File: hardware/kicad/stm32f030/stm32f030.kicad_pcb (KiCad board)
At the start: 2 copper layers, 29.6 x 10 mm, 89 parts, among them IC1 AT24CS02-SSHM, K1 RELAY_1RT, K2 RELAY_1RT, P1 5VIN, P10 SWD, P2 LOOP1, P3 LOOP2, P4 RELAY OUT 1, P5 TTL OUT 1, P6 RELAY OUT 2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

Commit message: hardware/kicad/stm32f030: blocks ready
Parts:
- C10, C14, C15, Q4, R10, R11, R12, R28: moved to B.Cu
- Y1: value 12MHz -> 8MHz; footprint Crystals:Crystal_SMD_3225_4Pads -> Crystals:Crystal_HC49-4H_Vertical
- moved K2 41.2 mm to (11.2, 150.4)
- moved LED2 41.1 mm to (15.7, 125.5)
- moved P7 41.1 mm to (11.7, 121.9)
- moved Q7 41.1 mm to (17.3, 130.0)
- moved Q8 41.1 mm to (17.3, 130.0)
- moved R20 41.1 mm to (20.3, 123.7)
- moved R21 41.1 mm to (15.7, 123.7)
- moved R22 41.1 mm to (20.3, 127.3)
- moved R23 41.1 mm to (20.3, 125.5)
- moved R24 41.1 mm to (15.7, 127.3)
- moved D2 41.1 mm to (23.1, 131.3)
- moved SW2 41.1 mm to (22.6, 121.2)
- moved P6 41.1 mm to (17.3, 158.0)
- moved P5 33.4 mm to (107.7, 125.1)
- moved D1 32.8 mm to (118.6, 131.6)
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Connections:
- P3 pad 1: Net-(GDT3-Pad2) -> Net-(GDT3-Pad1)
- P3 pad 3: Net-(GDT3-Pad1) -> Net-(GDT3-Pad2)
- R11 pad 1: /colpitts/osc1 -> /MCU/osc1
- R18 pad 2: /outputs/active1 -> /MCU/active1
- R23 pad 2: /MCU/active1 -> /MCU/active2
- R4 pad 1: /MCU/osc1 -> /MCU/osc2
- T2 pad 1: Net-(JP2-Pad2) -> Net-(C10-Pad1)
- T2 pad 3: Net-(C10-Pad1) -> Net-(JP2-Pad2)
- T2 pad 4: Net-(GDT3-Pad2) -> Net-(GDT3-Pad1)
- T2 pad 6: Net-(GDT3-Pad1) -> Net-(GDT3-Pad2)
- U2 pad 13: /colpitts/osc1 -> /MCU/osc2
- U2 pad 14: /outputs/active1 -> /MCU/active2
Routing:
- net +3V3: track 49.8 -> 19.0 mm
- net +5V: track 74.3 -> 91.4 mm, vias 1 -> 2
- net /MCU/active2: track 0.00 -> 16.5 mm, vias 0 -> 2
- net /MCU/active1: track 12.5 -> 0.40 mm, vias 1 -> 0
- net Net-(C15-Pad1): track 5.02 -> 16.4 mm
- net /colpitts/osc1: track 7.79 -> 0.00 mm, vias 1 -> 0
- net /MCU/osc2: track 0.00 -> 7.79 mm, vias 0 -> 1
- net Net-(JP3-Pad2): track 6.90 -> 14.6 mm
- net Net-(C10-Pad1): track 37.3 -> 30.5 mm, vias 0 -> 1
- net Net-(C14-Pad1): track 15.8 -> 11.2 mm
- net /MCU/reset: track 30.7 -> 26.3 mm, vias 2 -> 1
- net /outputs/active1: track 4.37 -> 0.00 mm, vias 1 -> 0
- net Net-(LED1-Pad1): track 14.1 -> 9.71 mm
- net Net-(Q4-Pad1): track 5.81 -> 1.58 mm
- net Net-(JP2-Pad2): track 24.3 -> 20.2 mm
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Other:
- board size 29.6 x 10 mm -> 103.5 x 10 mm

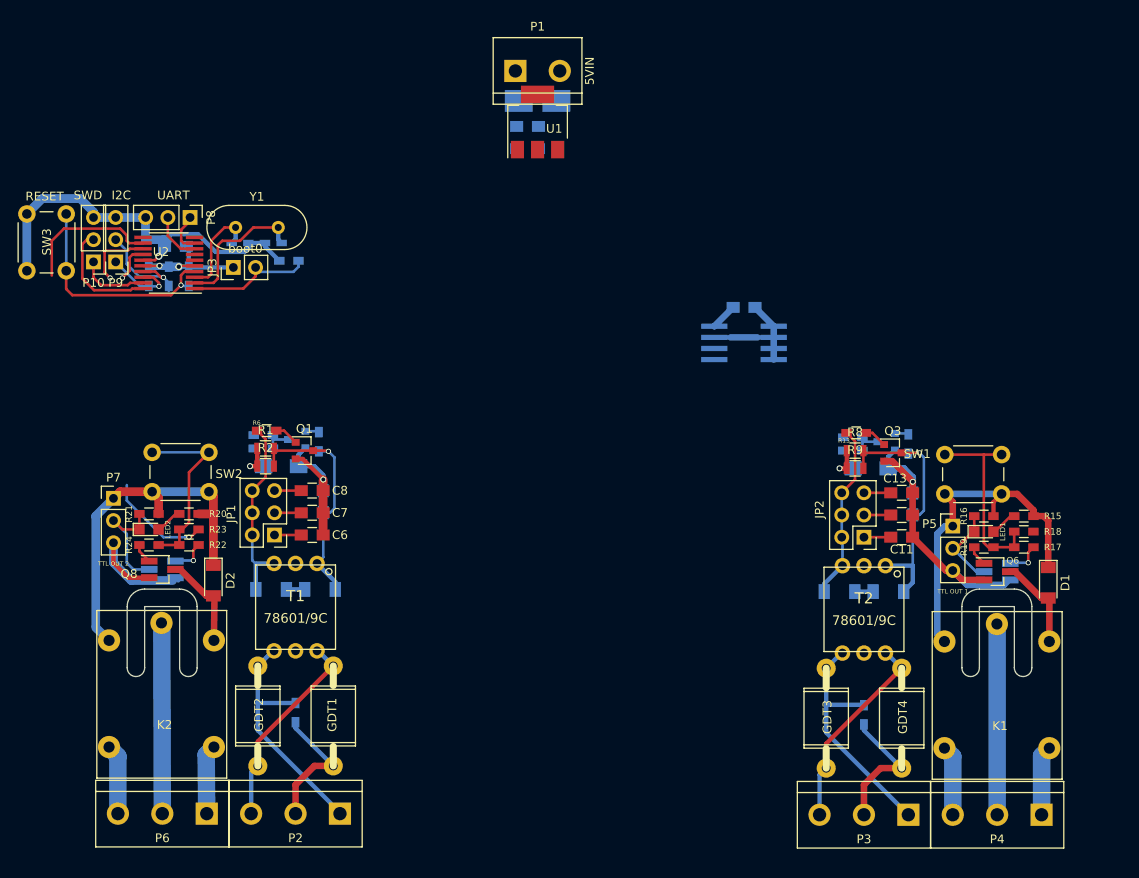
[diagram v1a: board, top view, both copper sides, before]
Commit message: hardware/kicad/stm32f030: everything is connected, DRC OK
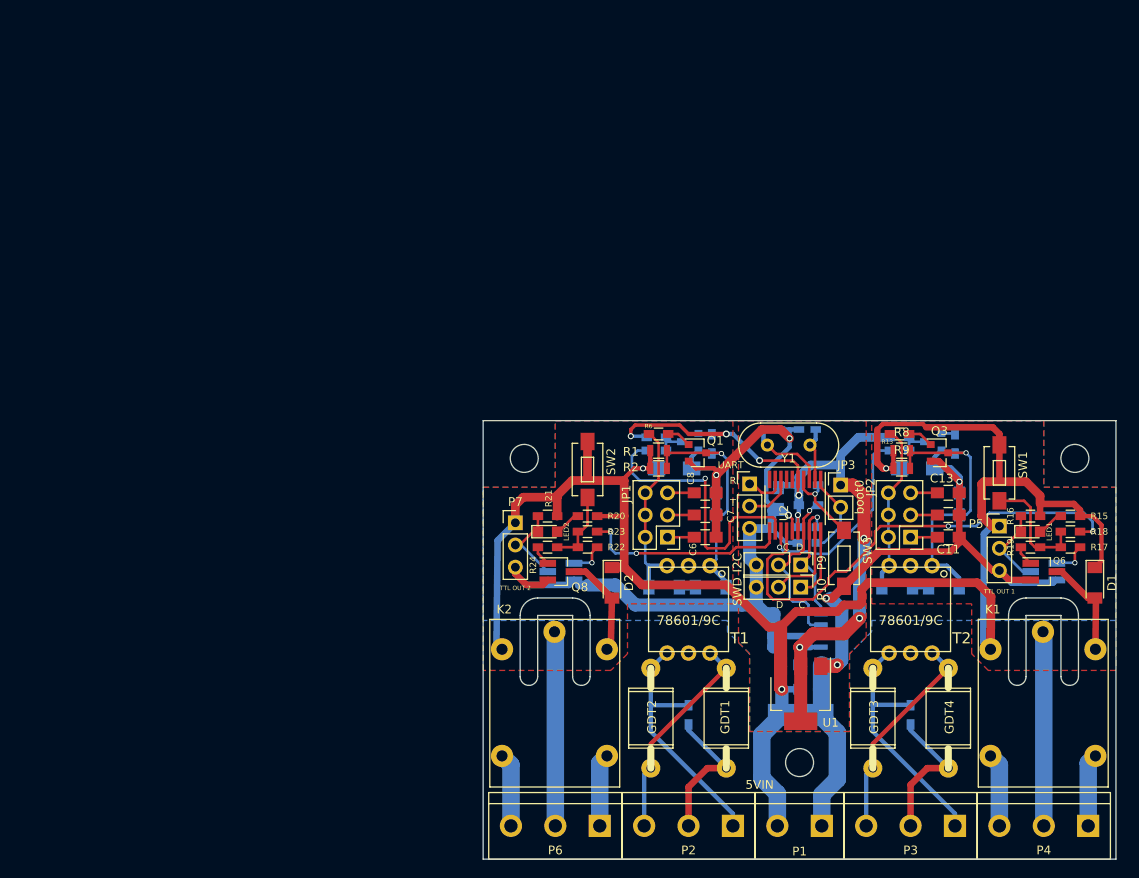
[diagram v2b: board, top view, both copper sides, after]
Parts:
- removed C18: 100n, Capacitors_SMD:C_0805_HandSoldering
- added REF**: MountingHole_3.2mm_M3, Mounting_Holes:MountingHole_3.2mm_M3, F.Cu at (90.2, 152.1)
- added REF**: MountingHole_3.2mm_M3, Mounting_Holes:MountingHole_3.2mm_M3, F.Cu at (121.7, 117.3)
- added REF**: MountingHole_3.2mm_M3, Mounting_Holes:MountingHole_3.2mm_M3, F.Cu at (58.7, 117.3)
- SW1, SW2: value TACTILE_SW -> SW_Push; footprint Buttons_Switches_THT:SW_PUSH_6mm -> cardetector:TS_362
- SW3: value RESET -> SW_Push; footprint Buttons_Switches_THT:SW_PUSH_6mm -> cardetector:TS_362
- moved SW3 99.1 mm to (95.2, 128.8), turned to 270 degrees
- moved P1 91.4 mm to (90.2, 159.4), turned to 180 degrees
- moved P10 89.0 mm to (90.3, 132.1), turned to 270 degrees
- moved P9 85.7 mm to (90.3, 129.5), turned to 270 degrees
- moved R27 80.6 mm to (91.1, 125.2), turned to 0 degrees
- moved R26 77.7 mm to (91.2, 122.7), turned to 0 degrees
- moved U2 76.8 mm to (89.7, 122.7), turned to 270 degrees
- moved C1 76.4 mm to (90.3, 146.7), turned to 0 degrees
- moved R25 74.8 mm to (91.2, 120.4), turned to 0 degrees
- moved C16 74.8 mm to (87.8, 121.9), turned to 270 degrees
- moved JP3 73.8 mm to (94.9, 120.4), turned to 0 degrees
- moved C2 72.1 mm to (91.4, 143.8), turned to 0 degrees
- moved U1 72.0 mm to (90.3, 144.3), turned to 270 degrees
- moved P8 70.9 mm to (84.5, 120.3), turned to 0 degrees
- moved R28 67.5 mm to (91.1, 127.0)
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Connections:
- P10 pad 1: /MCU/SWD -> /MCU/SWC
- P10 pad 2: /MCU/SWC -> /MCU/SWD
- R11 pad 1: /MCU/osc1 -> /MCU/osc2
- R18 pad 2: /MCU/active1 -> /MCU/active2
- R23 pad 2: /MCU/active2 -> /MCU/active1
- R4 pad 1: /MCU/osc2 -> /MCU/osc1
- SW3 pad 1: GND -> /MCU/reset
- SW3 pad 2: /MCU/reset -> GND
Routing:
- net +5V: track 91.4 -> 216.0 mm, vias 2 -> 3
- net +3V3: track 19.0 -> 91.4 mm, vias 2 -> 8
- net GND: track 135.4 -> 201.6 mm, vias 3 -> 6
- net /MCU/active2: track 16.5 -> 54.5 mm
- net /MCU/active1: track 0.40 -> 23.8 mm, vias 0 -> 2
- net /MCU/reset: track 26.3 -> 9.45 mm
- net /MCU/osc1: track 16.1 -> 32.8 mm, vias 0 -> 1
- net /MCU/osc2: track 7.79 -> 23.4 mm
- net Net-(R22-Pad2): track 21.1 -> 8.72 mm
- net Net-(C15-Pad1): track 16.4 -> 6.21 mm
- net Net-(R17-Pad2): track 22.0 -> 13.4 mm
- net /EEPROM/scl: track 12.7 -> 20.5 mm
- net /EEPROM/sda: track 9.10 -> 14.6 mm
- net /MCU/SWC: track 13.0 -> 8.12 mm
- net Net-(JP3-Pad2): track 14.6 -> 9.78 mm
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- added copper zone on F.Cu, net +3V3
- added copper zone on F.Cu, net +5V
- added copper zone on B.Cu, net GND
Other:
- board size 103.5 x 10 mm -> 72.4 x 50.2 mm
- board text added: "C"
- board text added: "D"
- board text added: "R"
- board text added: "T"

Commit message: hardware/kicad/stm32f030: final touches
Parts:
- moved REF** 0.28 mm to (121.9, 117.5)
- moved REF** 0.28 mm to (58.4, 117.5)
- moved C1 0.25 mm to (90.3, 146.9)
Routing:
- net /EEPROM/scl: track 20.5 -> 19.6 mm
- removed copper zone on F.Cu, net +3V3

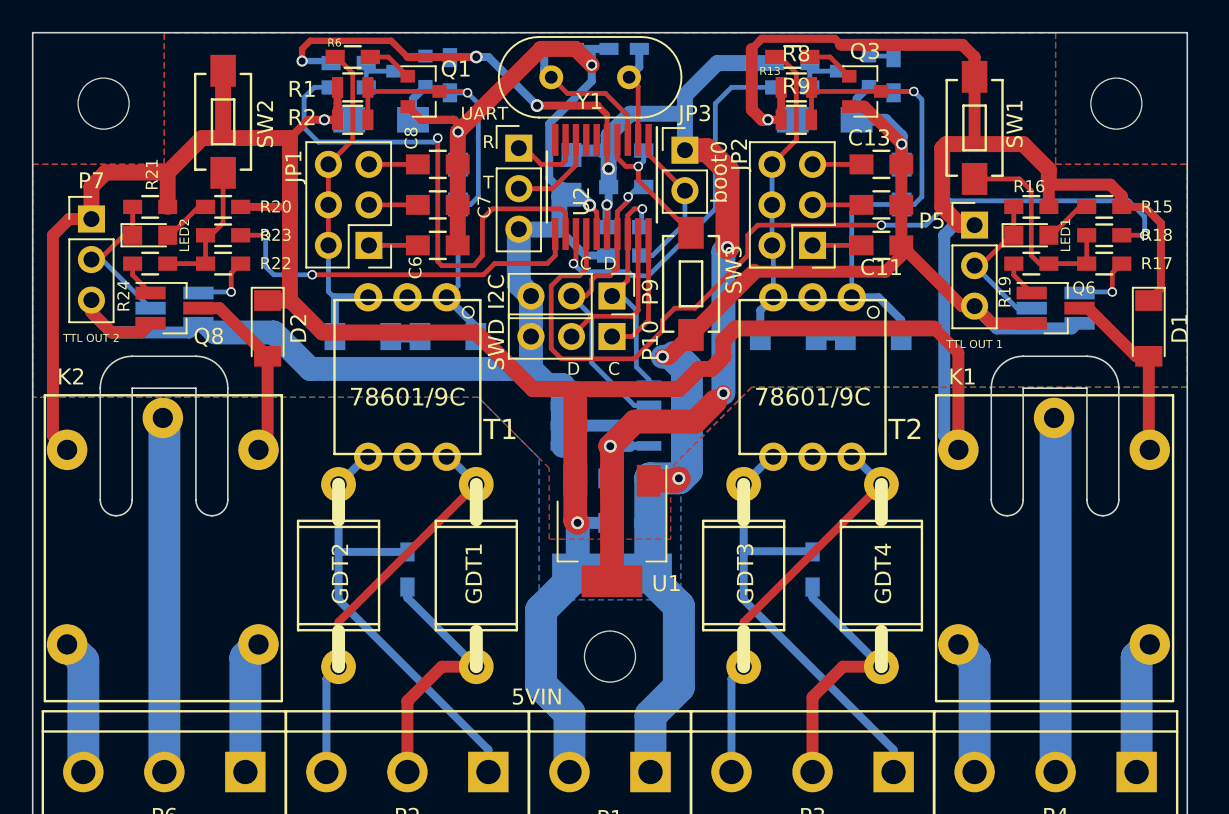
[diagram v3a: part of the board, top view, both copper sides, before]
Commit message: hardware/kicad/stm32f030: changed i2c bus and eeprom voltage to 5V
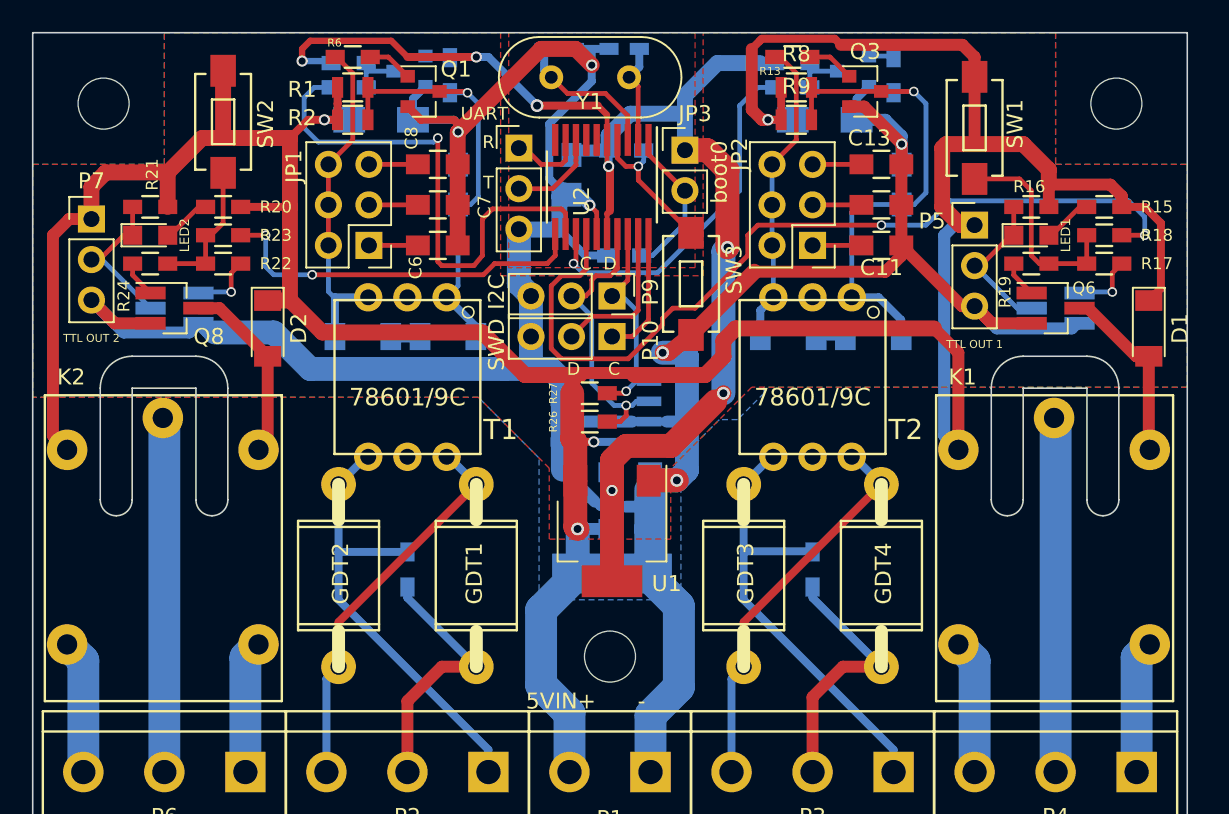
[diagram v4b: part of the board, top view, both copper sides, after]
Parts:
- P1: value 5VIN -> 5VIN+ -
- R26, R27: moved to F.Cu
- moved R26 14.9 mm to (88.9, 137.4)
- moved R27 10.6 mm to (88.9, 135.6)
- moved C2 0.38 mm to (91.4, 144.1)
- moved C3 0.38 mm to (91.4, 140.6)
- moved IC1 0.25 mm to (89.9, 136.8)
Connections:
- IC1 pad 8: +3V3 -> +5V
- R26 pad 1: +3V3 -> +5V
- R27 pad 1: +3V3 -> +5V
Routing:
- net GND: track 201.4 -> 210.5 mm
- net +5V: track 216.0 -> 221.6 mm, vias 3 -> 4
- net +3V3: track 91.5 -> 86.8 mm, vias 8 -> 7
- net /EEPROM/scl: track 19.6 -> 18.4 mm
- net /EEPROM/sda: track 14.6 -> 13.6 mm
- net /MCU/osc2: track 23.6 -> 22.7 mm
- added copper zone on F.Cu, net +3V3

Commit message: hardware/kicad/stm32f030: kicad version && lib bump
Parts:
- P1: value 5VIN+ - -> 5VIN
- U1: value LM1117-3.3 -> AP1117-33
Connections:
- U1 pad 4: +3V3 -> (no net)
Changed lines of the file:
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@@
-(kicad_pcb (version 4) (host pcbnew 4.0.6-e0-6349~52~ubuntu16.10.1)
+(kicad_pcb (version 4) (host pcbnew 4.0.7-e2-6376~58~ubuntu17.04.1)
   (general
-    (links 175)
+    (links 174)
     (no_connects 0)
     (area 53.924999 112.979999 126.415001 163.245001)
@@
   )
   (setup
-    (last_trace_width 0.4)
+    (last_trace_width 0.3)
     (user_trace_width 0.3)
     (user_trace_width 0.4)
@@
       (effects (font (size 1 1) (thickness 0.15)))
     )
-    (fp_text value "5VIN+      -" (at 1.524 4.445 180) (layer F.SilkS)
+    (fp_text value 5VIN (at 1.524 4.445 180) (layer F.SilkS)
       (effects (font (size 1 1) (thickness 0.15)))
     )
@@
       (effects (font (size 1 1) (thickness 0.15)))
     )
-    (fp_text value LM1117-3.3 (at 0 4.5 270) (layer F.Fab) hide
+    (fp_text value AP1117-33 (at 0 4.5 270) (layer F.Fab) hide
       (effects (font (size 1 1) (thickness 0.15)))
     )
@@
     (fp_line (start -1.85 3.35) (end 1.85 3.35) (layer F.Fab) (width 0.15))
     (fp_line (start 1.85 -3.35) (end 1.85 3.35) (layer F.Fab) (width 0.15))
-    (pad 4 smd rect (at 3.15 0 270) (size 2 3.8) (layers F.Cu F.Paste F.Mask)
-      (net 3 +3V3))
+    (pad 4 smd rect (at 3.15 0 270) (size 2 3.8) (layers F.Cu F.Paste F.Mask))
     (pad 2 smd rect (at -3.15 0 270) (size 2 1.5) (layers F.Cu F.Paste F.Mask)
       (net 3 +3V3))
